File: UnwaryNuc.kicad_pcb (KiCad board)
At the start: 4 copper layers, 125.3 x 66.8 mm, 173 parts, among them J1 USB_B_Micro, J2 USB_A_Dual, J3 Conn_01x06_Male, J4 RJ45_Amphenol_RJMG1BD3B8K1ANR, J5 RJ45_Amphenol_RJMG1BD3B8K1ANR, J6 Conn_02x04_Odd_Even, Q1 2N3904, Q2 BC856BDW1, SW1 SW_SPST, U1 NUC980DF71YC, U2 LAN8740A-EN-TR, U3 LAN8740A-EN-TR, U4 LD3985M18R_TSOT23, U5 MIC4690, U6 LM3880, U7 AP2127K-1.2, U8 S25FL127SABMFV100, X1 ASE-xxxMHz, X2 ASE-xxxMHz, Y1 ABS07-166, Y2 NX5032GA

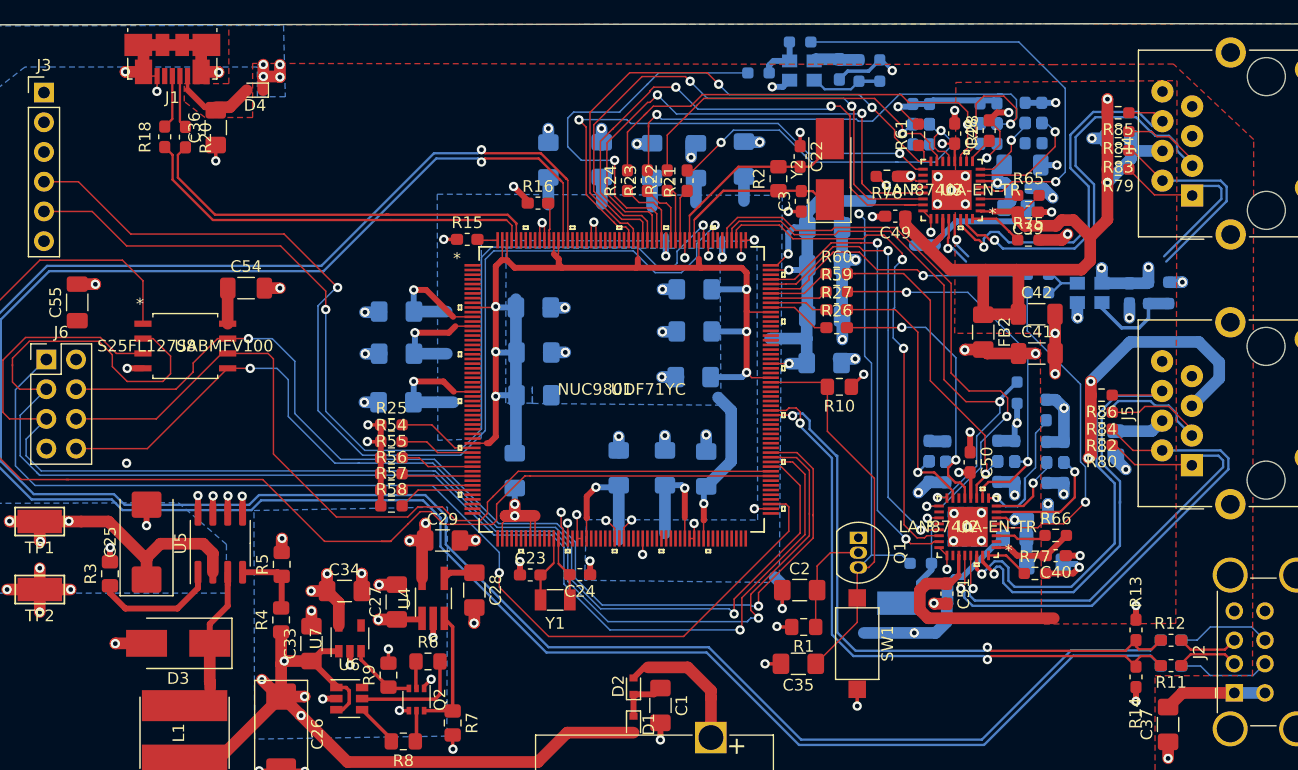
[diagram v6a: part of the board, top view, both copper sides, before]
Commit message: finished up some power routing, could still use some cleanup. need to add header for esp and additional GPIO header/expander
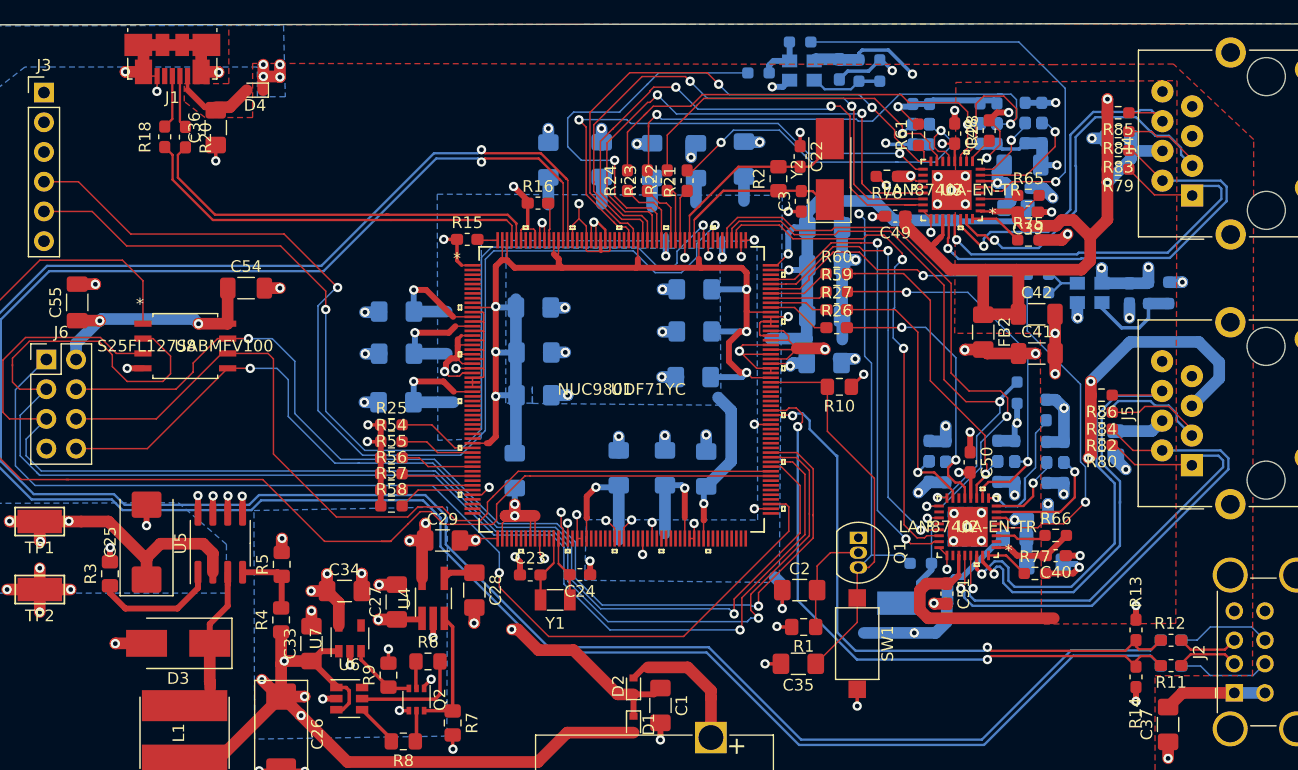
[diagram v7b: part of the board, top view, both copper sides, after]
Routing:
- net +1V2: track 162.7 -> 280.0 mm
- net +3V3: track 238.7 -> 329.3 mm, vias 27 -> 31
- net +1V8: track 6.18 -> 90.2 mm, vias 2 -> 4
- net GND: track 200.1 -> 269.5 mm, vias 112 -> 120
- net /VDD_RTC: track 4.39 -> 26.8 mm, vias 0 -> 2
- net /P0.1N: track 22.8 -> 39.7 mm
- net /P0.1P: track 20.8 -> 37.1 mm
- net /P0.0N: track 35.3 -> 31.1 mm
- net /P0.0P: track 41.1 -> 38.0 mm
- net /QSPI0_SS0: vias 1 -> 0
- added copper zone on L2_(Plane), net +3V3
- added copper zone on L3_(Sig), net GND
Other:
- net class Default: clearance 0.2 -> 0.127
- rule trace_clearance: 0.2 -> 0.127

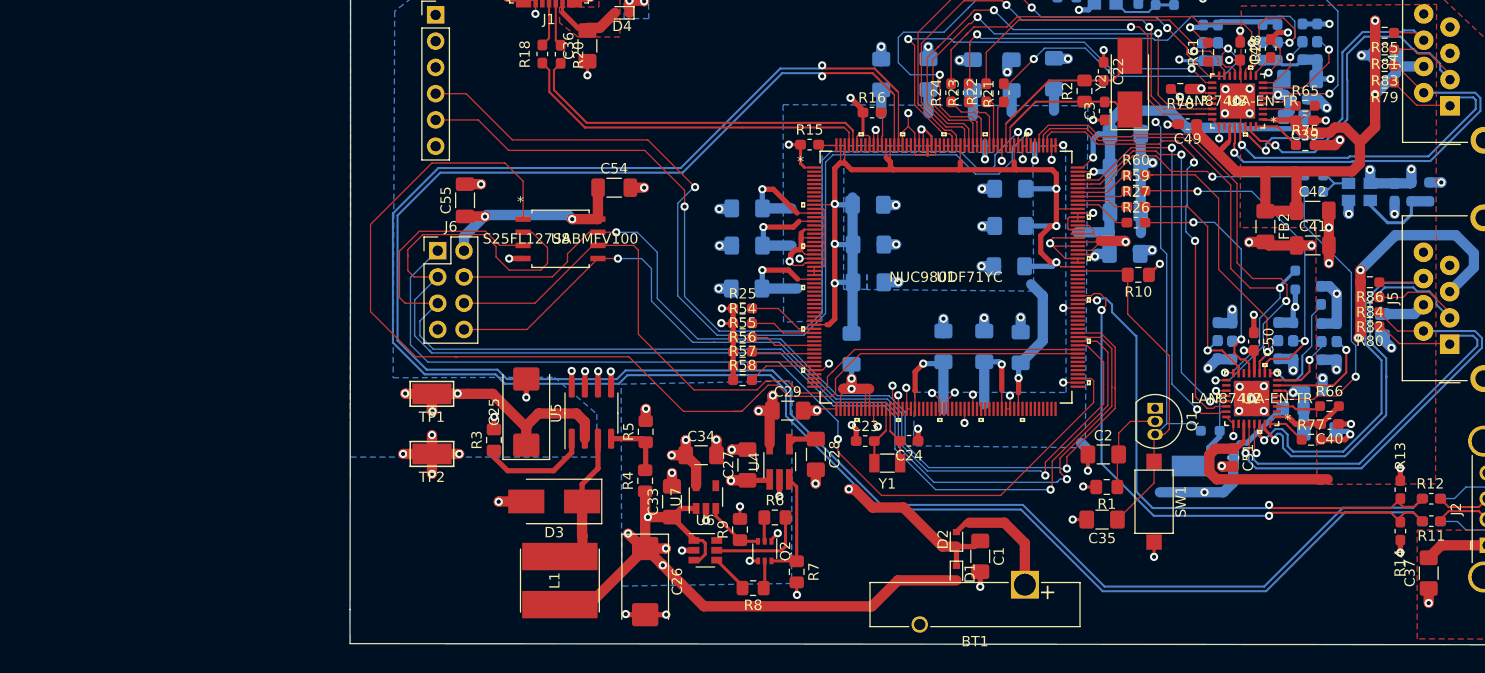
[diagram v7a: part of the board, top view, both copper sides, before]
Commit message: added two spi headers, I2C, and a bank of GPIO. placed, still need routed
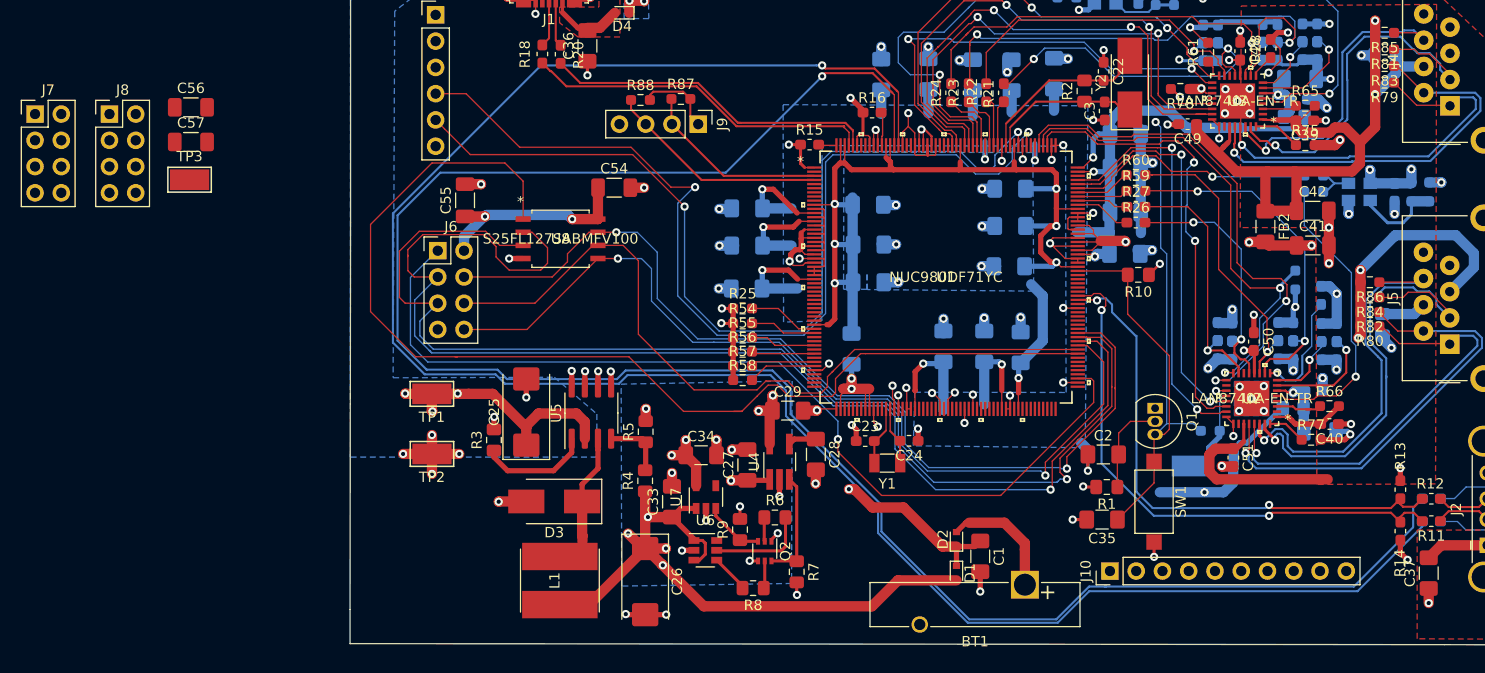
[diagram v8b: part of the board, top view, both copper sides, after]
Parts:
- added C56: 0.1u, Capacitor_SMD:C_1206_3216Metric_Pad1.33x1.80mm_HandSolder, F.Cu at (67.3, 74.6)
- added C57: 0.1u, Capacitor_SMD:C_1206_3216Metric_Pad1.33x1.80mm_HandSolder, F.Cu at (67.3, 77.9)
- added J10: Conn_01x10_Male, Connector_PinHeader_2.54mm:PinHeader_1x10_P2.54mm_Vertical, F.Cu at (156.2, 119.4)
- added J7: Conn_02x04_Odd_Even, Connector_PinHeader_2.54mm:PinHeader_2x04_P2.54mm_Vertical, F.Cu at (52.2, 75.2)
- added J8: Conn_02x04_Odd_Even, Connector_PinHeader_2.54mm:PinHeader_2x04_P2.54mm_Vertical, F.Cu at (59.4, 75.2)
- added J9: Conn_01x04_Male, Connector_PinHeader_2.54mm:PinHeader_1x04_P2.54mm_Vertical, F.Cu at (116.3, 76.2)
- added R87: 4.7k, Resistor_SMD:R_0603_1608Metric_Pad0.98x0.95mm_HandSolder, F.Cu at (114.7, 73.8)
- added R88: 4.7k, Resistor_SMD:R_0603_1608Metric_Pad0.98x0.95mm_HandSolder, F.Cu at (110.7, 73.9)
- added TP3: TestPoint, TestPoint:TestPoint_Keystone_5019_Minature, F.Cu at (67.1, 81.6)
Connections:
- U1 pad 3: Net-(U1-Pad3) -> /SDA0
- U1 pad 4: Net-(U1-Pad4) -> /SCL0
- U1 pad 52: Net-(U1-Pad52) -> /PB0
- U1 pad 53: Net-(U1-Pad53) -> /PB6
- U1 pad 54: Net-(U1-Pad54) -> /PB4
- U1 pad 57: Net-(U1-Pad57) -> /PB7
- U1 pad 58: Net-(U1-Pad58) -> /PB5
- U1 pad 59: Net-(U1-Pad59) -> /PB1
- U1 pad 60: Net-(U1-Pad60) -> /PB3
- U1 pad 61: Net-(U1-Pad61) -> /PB2
- U1 pad 75: Net-(U1-Pad75) -> /SPI0_SS1
- U1 pad 81: Net-(U1-Pad81) -> /SPIO_SS0
- U1 pad 83: Net-(U1-Pad83) -> /SPI0_CLK
- U1 pad 84: Net-(U1-Pad84) -> /SPI0_MOSI
- U1 pad 85: Net-(U1-Pad85) -> /SPI0_MISO
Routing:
- net +3V3: track 329.3 -> 365.9 mm
- net /SCL0: track 0.00 -> 21.5 mm
- net /SDA0: track 0.00 -> 18.3 mm
- net /USB1_P: track 186.7 -> 191.9 mm
- net /USB1_N: track 188.8 -> 192.3 mm
- net /USB0.DD_N: track 35.1 -> 32.6 mm
- net +1V8: track 90.2 -> 92.3 mm
- net GND: track 269.5 -> 270.9 mm
- net /USB0.DD_P: track 35.0 -> 33.8 mm
- net /UART0_TXD: track 90.8 -> 89.8 mm
- net /QSPI0_CLK: track 75.6 -> 75.0 mm
